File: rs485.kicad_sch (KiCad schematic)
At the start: 21 parts

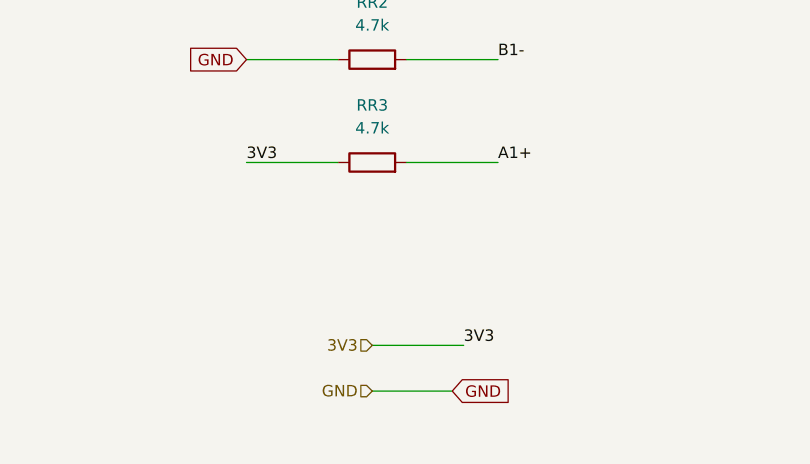
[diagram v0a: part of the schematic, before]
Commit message: feat: integrated rtc ldc i2c / fixed 12v power line rs485 / output com pin -> input power type
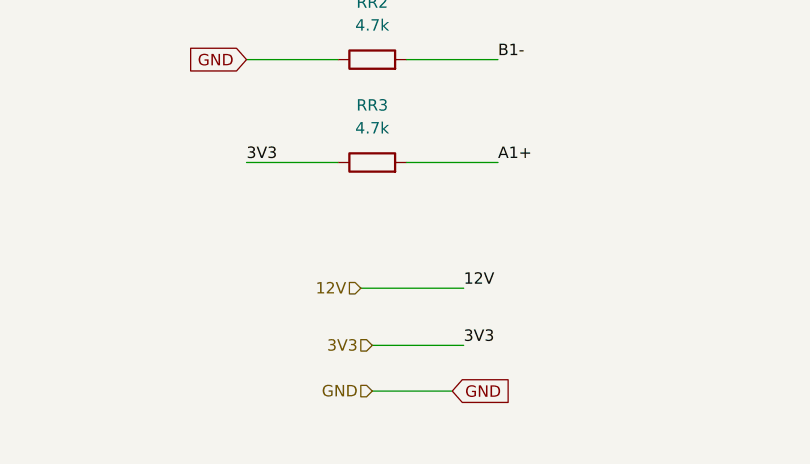
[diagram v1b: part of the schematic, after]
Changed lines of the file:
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@@
+	(wire
+		(pts
+			(xy 82.55 130.81) (xy 93.98 130.81)
+		)
+		(stroke
+			(width 0)
+			(type default)
+		)
+	)
 	(wire
 		(pts
@@
 	(label "GND"
 		(at 43.18 48.26 0)
+		(effects
+			(font
+				(size 1.27 1.27)
+			)
+			(justify left bottom)
+		)
+	)
+	(label "12V"
+		(at 93.98 130.81 0)
 		(effects
 			(font
@@
 		(effects
 			(font
+				(size 1.27 1.27)
+			)
+			(justify right)
+		)
+	)
+	(hierarchical_label "12V"
+		(shape input)
+		(at 82.55 130.81 180)
+		(effects
+			(font

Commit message: feat: position of the components improved
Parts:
- DR4, DR8: footprint Diode_SMD:D_SOD-323 -> Diode_SMD:D_SMA_Handsoldering
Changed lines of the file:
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@@
 			)
 		)
-		(property "Footprint" "Diode_SMD:D_SOD-323"
+		(property "Footprint" "Diode_SMD:D_SMA_Handsoldering"
 			(at 190.5 74.295 0)
 			(effects
@@
 			)
 		)
-		(property "Footprint" "Diode_SMD:D_SOD-323"
+		(property "Footprint" "Diode_SMD:D_SMA_Handsoldering"
 			(at 60.96 73.025 0)
 			(effects

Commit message: tarjeta para raspberri, pdfs y relacion de pines
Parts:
- DR4, DR8: footprint Diode_SMD:D_SMA_Handsoldering -> Diode_SMD:D_SOD-323
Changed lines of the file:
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@@
 			)
 		)
-		(property "Footprint" "Diode_SMD:D_SMA_Handsoldering"
+		(property "Footprint" "Diode_SMD:D_SOD-323"
 			(at 190.5 74.295 0)
 			(effects
@@
 			)
 		)
-		(property "Footprint" "Diode_SMD:D_SMA_Handsoldering"
+		(property "Footprint" "Diode_SMD:D_SOD-323"
 			(at 60.96 73.025 0)
 			(effects
